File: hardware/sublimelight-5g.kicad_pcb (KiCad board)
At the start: 2 copper layers, 75 x 85 mm, 36 parts, among them J1 RJ45, J2 RJ45, J3 Barrel_Jack_Switch, J4 Conn_01x04, J5 Conn_01x05, J6 Barrel_Jack_Switch, J7 Conn_01x05, J8 Conn_01x02, SW1 SW_Push, U1 ST1480ACDR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

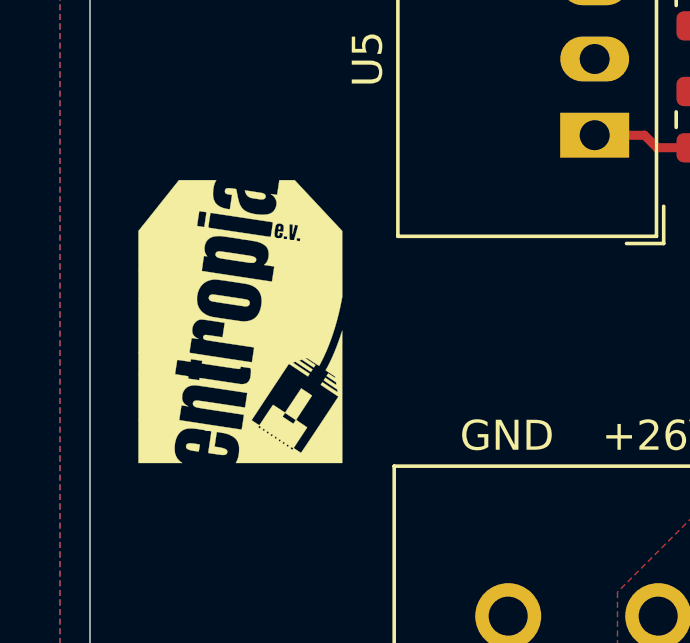
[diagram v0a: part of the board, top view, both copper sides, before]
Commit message: replace +28V power supply symbol with VCC symbol
VCC is +26V
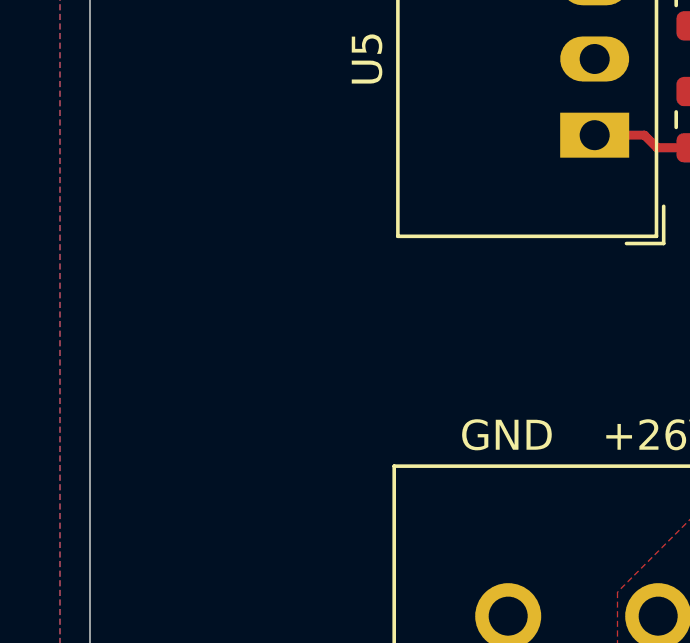
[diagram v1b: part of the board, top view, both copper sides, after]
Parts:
- removed G***: LOGO, logos:entropia
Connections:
- net +28V renamed VCC

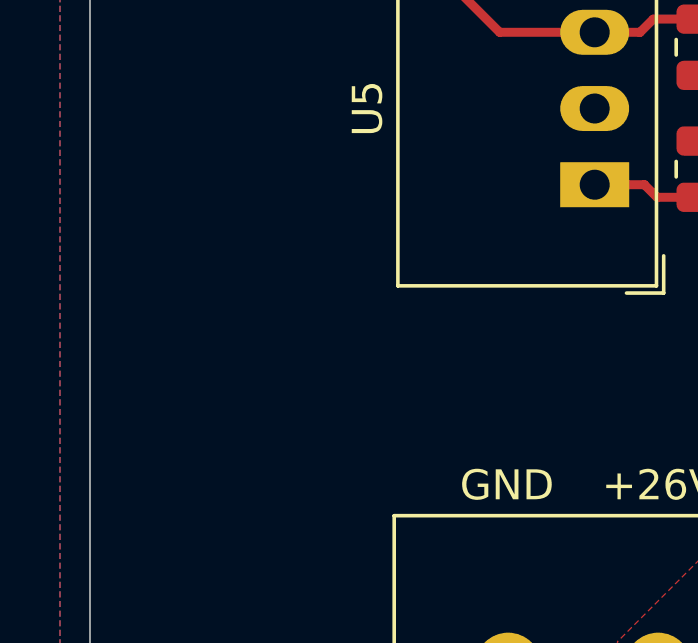
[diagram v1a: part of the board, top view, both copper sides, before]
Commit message: add logos to board
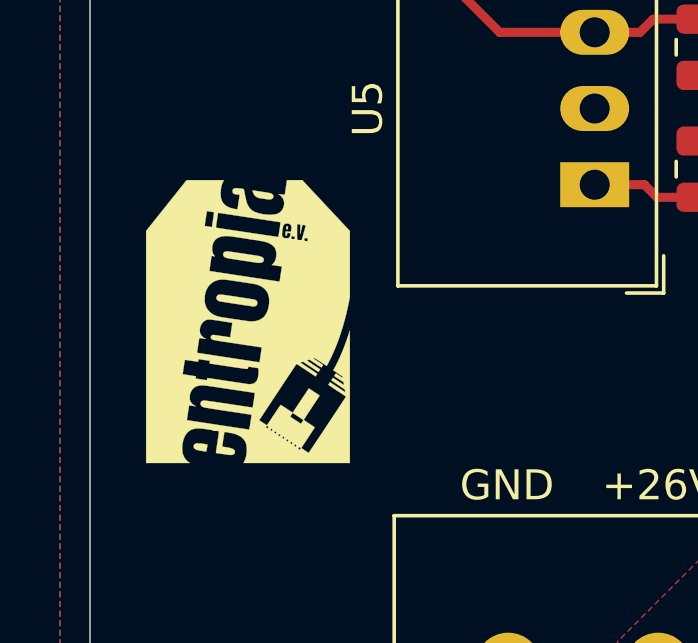
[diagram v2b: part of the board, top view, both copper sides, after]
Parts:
- added G***: LOGO, logos:entropia, B.Cu at (118.6, 110.7)
- added G***: LOGO, logos:entropia, F.Cu at (80.3, 111.1)
